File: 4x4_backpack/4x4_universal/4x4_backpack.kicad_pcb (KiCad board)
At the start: 2 copper layers, 76.2 x 76.2 mm, 46 parts, among them J1 Conn_01x04, J11 Conn_01x01, J12 Conn_01x01, J13 Conn_01x01, J14 Conn_01x01, J15 Conn_01x01, J16 Conn_01x01, J2 Conn_01x04, J3 Conn_01x04, J4 Conn_01x04, J5 Conn_01x04, J6 Conn_01x04, J7 Conn_01x04, J8 Conn_01x04

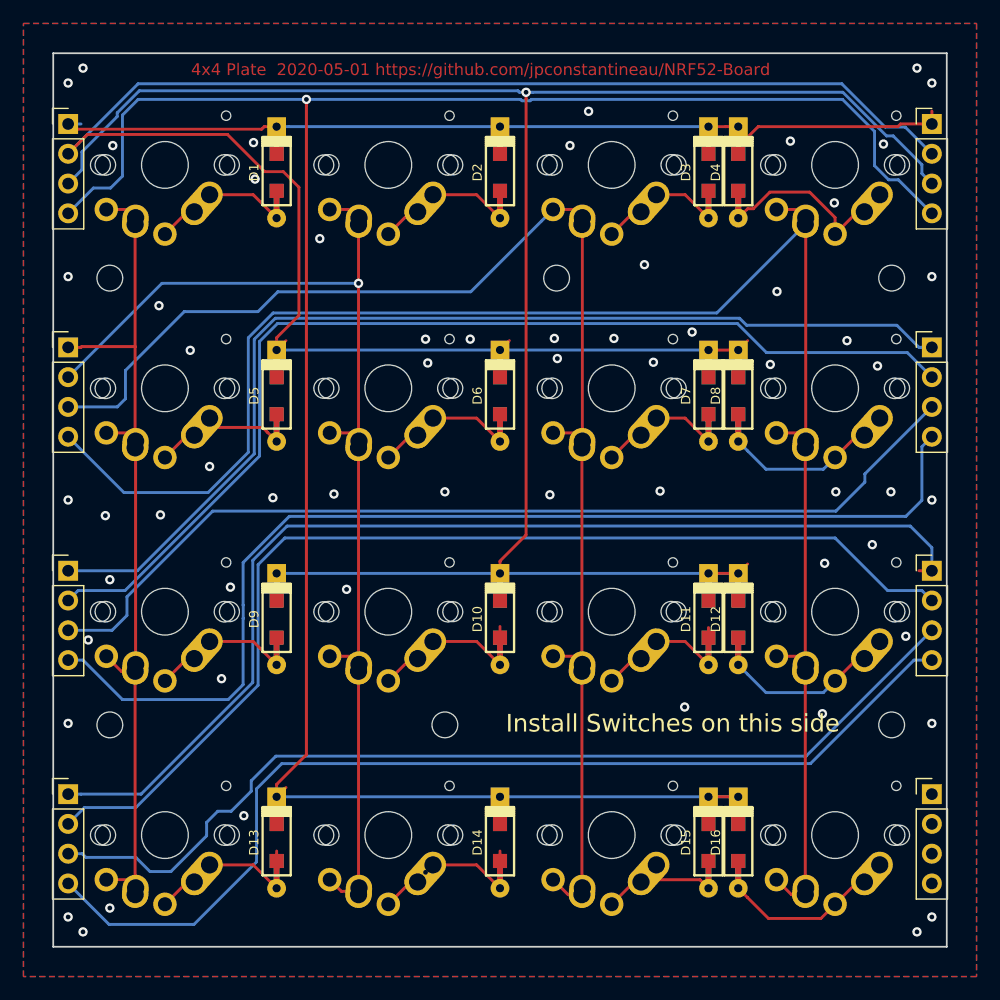
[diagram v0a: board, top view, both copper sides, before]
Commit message: adding BlueMicro840
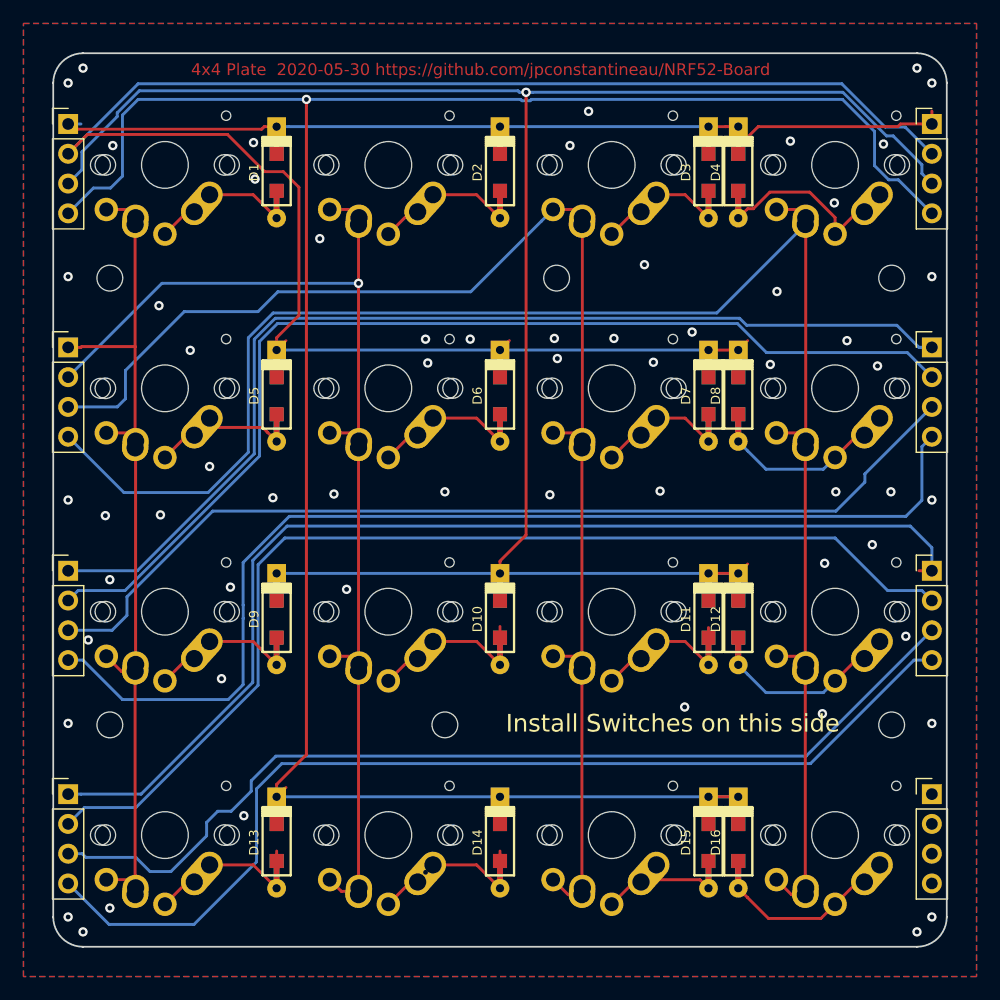
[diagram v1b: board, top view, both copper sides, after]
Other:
- outline, holes or cut-outs redrawn
- board text added: "4x4 Plate 2020-05-30 https://github.com/jpconstantineau/NRF52-Board"
- board text removed: "4x4 Plate 2020-05-01 https://github.com/jpconstantineau/NRF52-Board"
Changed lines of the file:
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@@
   (general
     (thickness 1.6)
-    (drawings 48)
+    (drawings 52)
     (tracks 399)
     (zones 0)
@@
   (page A4)
   (layers
-    (0 F.Cu signal hide)
-    (31 B.Cu signal hide)
+    (0 F.Cu signal)
+    (31 B.Cu signal)
     (32 B.Adhes user)
     (33 F.Adhes user)
@@
     (38 B.Mask user)
     (39 F.Mask user)
-    (40 Dwgs.User user)
+    (40 Dwgs.User user hide)
     (41 Cmts.User user)
     (42 Eco1.User user hide)
@@
     (pad_to_mask_clearance 0.2)
     (aux_axis_origin 0 0)
+    (grid_origin 76.2 76.2)
     (visible_elements 7FFFFFFF)
     (pcbplotparams
@@
     (pad "" np_thru_hole circle (at -5.22 4.2 228.1) (size 0.8 0.8) (drill 0.8) (layers *.Cu *.Mask))
   )
+  (gr_arc (start 78.74 149.86) (end 76.2 149.86) (angle -90) (layer Edge.Cuts) (width 0.15))
+  (gr_arc (start 149.86 149.86) (end 149.86 152.4) (angle -90) (layer Edge.Cuts) (width 0.15))
+  (gr_arc (start 149.86 78.74) (end 152.4 78.74) (angle -90) (layer Edge.Cuts) (width 0.15))
+  (gr_arc (start 78.74 78.74) (end 78.74 76.2) (angle -90) (layer Edge.Cuts) (width 0.15))
   (gr_text "Cols after" (at 141.605 119.253) (layer B.SilkS)
     (effects (font (size 1.5 1.5) (thickness 0.3)) (justify mirror))
@@
     (effects (font (size 1.5 1.5) (thickness 0.3)))
   )
-  (gr_text "4x4 Plate  2020-05-01 https://github.com/jpconstantineau/NRF52-Board" (at 112.649 77.597) (layer F.Cu)
+  (gr_text "4x4 Plate  2020-05-30 https://github.com/jpconstantineau/NRF52-Board" (at 112.649 77.597) (layer F.Cu)
     (effects (font (size 1 1) (thickness 0.2)))
   )
@@
   (gr_line (start 151.13 74.93) (end 151.13 153.67) (layer Dwgs.User) (width 0.2))
   (gr_line (start 77.47 74.93) (end 77.47 153.67) (layer Dwgs.User) (width 0.2))
-  (gr_line (start 152.4 76.2) (end 76.2 76.2) (layer Edge.Cuts) (width 0.15))
-  (gr_line (start 152.4 152.4) (end 152.4 76.2) (layer Edge.Cuts) (width 0.15))
-  (gr_line (start 76.2 152.4) (end 152.4 152.4) (layer Edge.Cuts) (width 0.15))
-  (gr_line (start 76.2 76.2) (end 76.2 152.4) (layer Edge.Cuts) (width 0.15))
+  (gr_line (start 149.86 76.2) (end 78.74 76.2) (layer Edge.Cuts) (width 0.15))
+  (gr_line (start 152.4 149.86) (end 152.4 78.74) (layer Edge.Cuts) (width 0.15))
+  (gr_line (start 78.74 152.4) (end 149.86 152.4) (layer Edge.Cuts) (width 0.15))
+  (gr_line (start 76.2 78.74) (end 76.2 149.86) (layer Edge.Cuts) (width 0.15))
   (segment (start 77.47 82.2325) (end 78.57 82.2325) (width 0.25) (layer B.Cu) (net 1) (status 10))
   (segment (start 95.25 83.66) (end 95.25 82.66) (width 0.25) (layer F.Cu) (net 1) (status 30))
@@
   (segment (start 102.235 90.265) (end 102.235 95.8215) (width 0.25) (layer F.Cu) (net 16))
   (segment (start 102.235 95.8215) (end 102.235 109.855) (width 0.25) (layer F.Cu) (net 16))
-  (via (at 126.365 146.685) (size 0.8) (drill 0.4) (layers F.Cu B.Cu) (net 32) (status 30))
-  (via (at 107.95 146.05) (size 0.8) (drill 0.4) (layers F.Cu B.Cu) (net 31) (status 30))
   (segment (start 77.47 101.2825) (end 77.7875 100.965) (width 0.25) (layer B.Cu) (net 17) (status 30))
   (segment (start 83.185 90.17) (end 83.185 90.805) (width 0.25) (layer F.Cu) (net 17))
@@
   (segment (start 93.255 145.415) (end 95.25 147.41) (width 0.25) (layer F.Cu) (net 30))
   (segment (start 89.535 145.415) (end 93.255 145.415) (width 0.25) (layer F.Cu) (net 30))
+  (via (at 107.95 146.05) (size 0.8) (drill 0.4) (layers F.Cu B.Cu) (net 31) (status 30))
   (segment (start 114.3 144.235) (end 114.3 145.085) (width 0.25) (layer F.Cu) (net 31) (status 20))
   (segment (start 108.135 145.415) (end 108.585 145.415) (width 0.25) (layer F.Cu) (net 31))
@@
   (segment (start 112.305 145.415) (end 114.3 147.41) (width 0.25) (layer F.Cu) (net 31))
   (segment (start 108.585 145.415) (end 112.305 145.415) (width 0.25) (layer F.Cu) (net 31))
+  (via (at 126.365 146.685) (size 0.8) (drill 0.4) (layers F.Cu B.Cu) (net 32) (status 30))
   (segment (start 125.725 146.875) (end 126.325 146.875) (width 0.25) (layer F.Cu) (net 32))
   (segment (start 123.825 148.775) (end 125.725 146.875) (width 0.25) (layer F.Cu) (net 32))

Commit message: added BlueHand to docs
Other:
- outline, holes or cut-outs redrawn
- board text added: "4x4 Plate 2021-02-07 https://github.com/jpconstantineau/NRF52-Board"
- board text removed: "4x4 Plate 2020-05-30 https://github.com/jpconstantineau/NRF52-Board"
